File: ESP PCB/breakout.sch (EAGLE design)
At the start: 9 parts, among them X1 53047-04, X2 53047-04, X3 53047-04, X4 53047-04

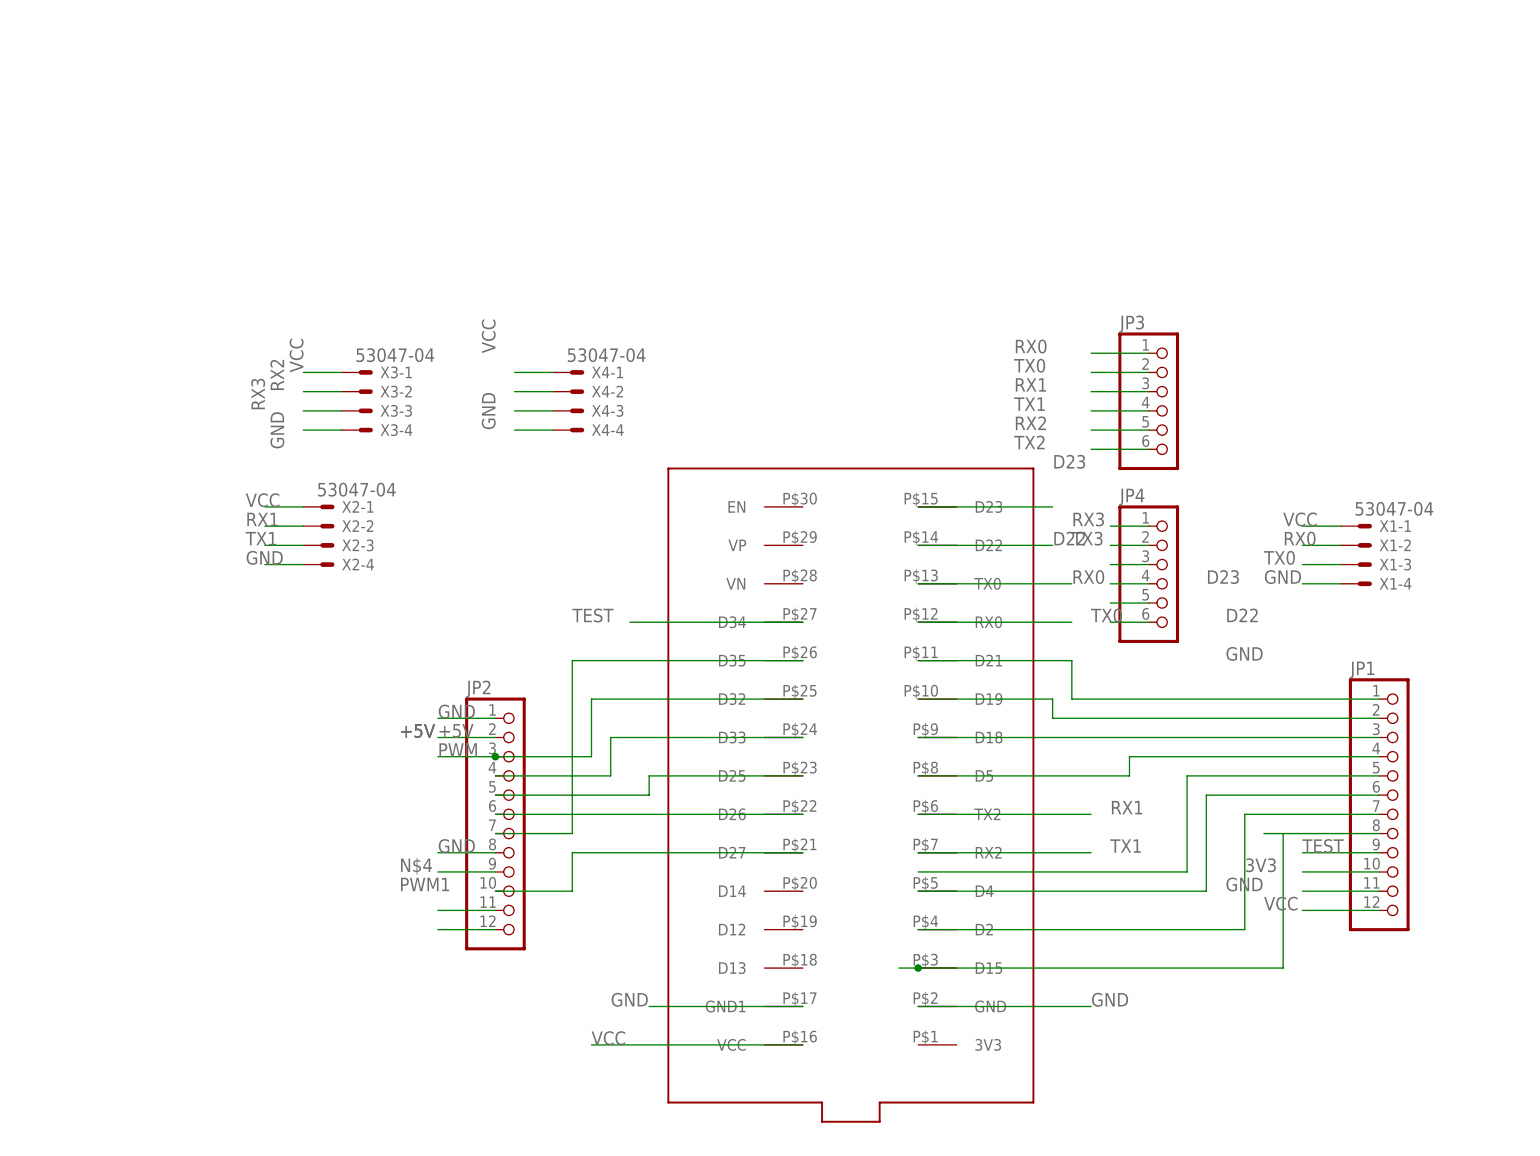
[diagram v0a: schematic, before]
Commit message: update pcb remove cam
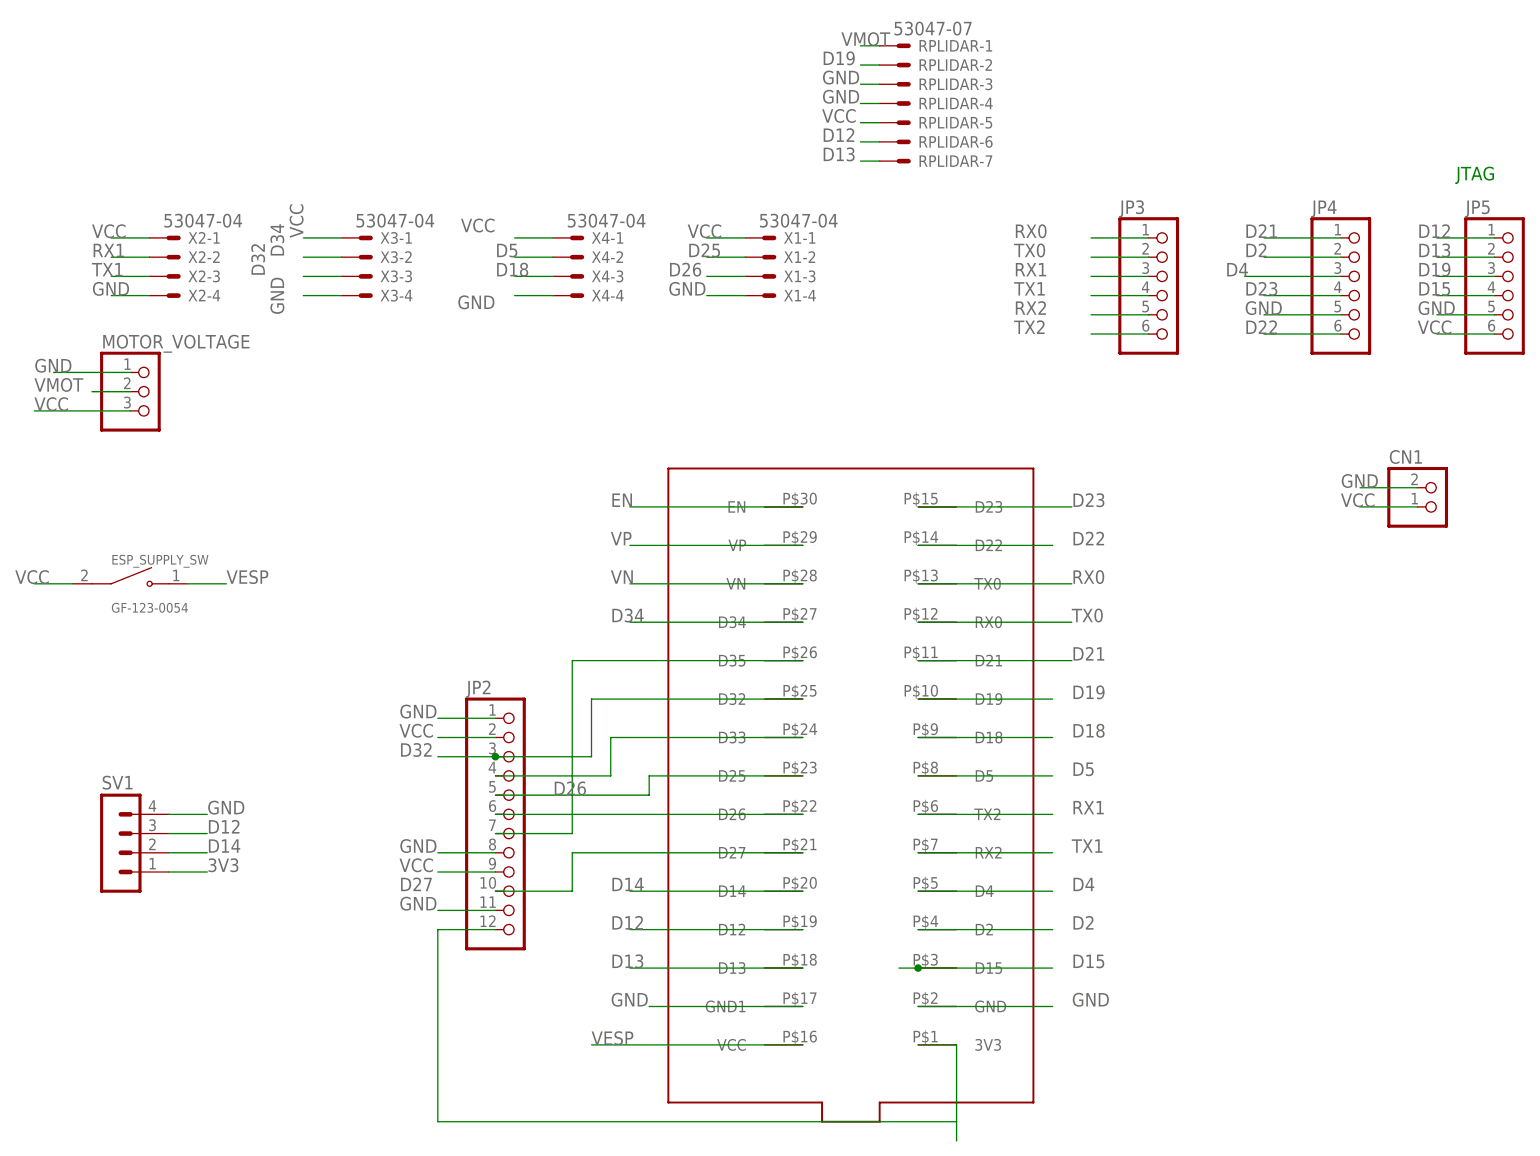
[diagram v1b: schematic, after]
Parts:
- removed JP1: (no value), adafruit:PINHD-1X12
- added CN1: (no value), adafruit:JST_2PIN-THM
- added ESP_SUPPLY_SW: GF-123-0054, GF-123-0054:GF-123-0054
- added JP5: (no value), adafruit:PINHD-1X6
- added MOTOR_VOLTAGE: (no value), adafruit:PINHD-1X3
- added RPLIDAR: 53047-07, con-molex:53047-07
- added SV1: (no value), con-lstb:MA04-1
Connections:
- net PWM1 renamed D27
- removed net +5V: JP2.2
- removed net N$10: JP1.3, U$1.D18
- removed net N$11: JP1.4, U$1.D5
- removed net N$12: JP1.5
- removed net N$13: JP1.6, U$1.D4
- removed net N$14: JP1.7, U$1.D2
- removed net N$15: JP1.8, U$1.D15
- removed net N$2: JP2.11
- removed net N$22: JP4.3
- removed net N$4: JP2.9
- removed net N$5: JP1.1, U$1.D21
- removed net N$7: JP2.5, U$1.D25
- removed net N$8: JP2.6, U$1.D26
- removed net N$9: JP1.2, U$1.D19
- removed net PWM: JP2.3, U$1.D32
- removed net RX3: JP4.1, X3-3.S, X4-2.S
- removed net TEST: JP1.9, U$1.D34
- removed net TX3: JP4.2, X4-3.S
- new net D12: JP5.1, RPLIDAR-6.S, SV1.3, U$1.D12
- new net D13: JP5.2, RPLIDAR-7.S, U$1.D13
- new net D14: SV1.2, U$1.D14
- new net D15: JP5.4, U$1.D15
- new net D18: U$1.D18, X4-3.S
- new net D19: JP5.3, RPLIDAR-2.S, U$1.D19
- new net D2: JP4.2, U$1.D2
- new net D21: JP4.1, U$1.D21
- new net D25: JP2.5, U$1.D25, X1-2.S
- new net D26: JP2.6, U$1.D26, X1-3.S
- new net D32: JP2.3, U$1.D32, X3-3.S
- new net D34: U$1.D34, X3-2.S
- new net D4: JP4.3, U$1.D4
- new net D5: U$1.D5, X4-2.S
- new net EN: U$1.EN
- new net VESP: ESP_SUPPLY_SW.1, U$1.VCC
- new net VMOT: MOTOR_VOLTAGE.2, RPLIDAR-1.S
- new net VN: U$1.VN
- new net VP: U$1.VP
- net 3V3: now also SV1.1; no longer JP1.10
- net GND: now also CN1.1, JP2.11, JP5.5, MOTOR_VOLTAGE.1, RPLIDAR-3.S, RPLIDAR-4.S, SV1.4; no longer JP1.11
- net N$1: now also U$1.3V3
- net RX0: no longer X1-2.S
- net RX2: no longer X3-2.S
- net TX0: no longer X1-3.S
- net VCC: now also CN1.2, ESP_SUPPLY_SW.2, JP2.2, JP2.9, JP5.6, MOTOR_VOLTAGE.3, RPLIDAR-5.S; no longer JP1.12, U$1.VCC
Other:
- note added: "JTAG"
- moved on the sheet: JP3, JP4, X1-1, X1-2, X1-3, X1-4, X2-1, X2-2, X2-3, X2-4, X3-1, X3-2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
